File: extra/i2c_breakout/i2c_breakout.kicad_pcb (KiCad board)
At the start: 2 copper layers, 39.5 x 34.6 mm, 7 parts, among them J1 Conn_01x04_Socket, J2 Conn_01x04_Socket, J3 Conn_01x04_Socket, J4 Conn_01x04_Socket, U2 TLV1117-33

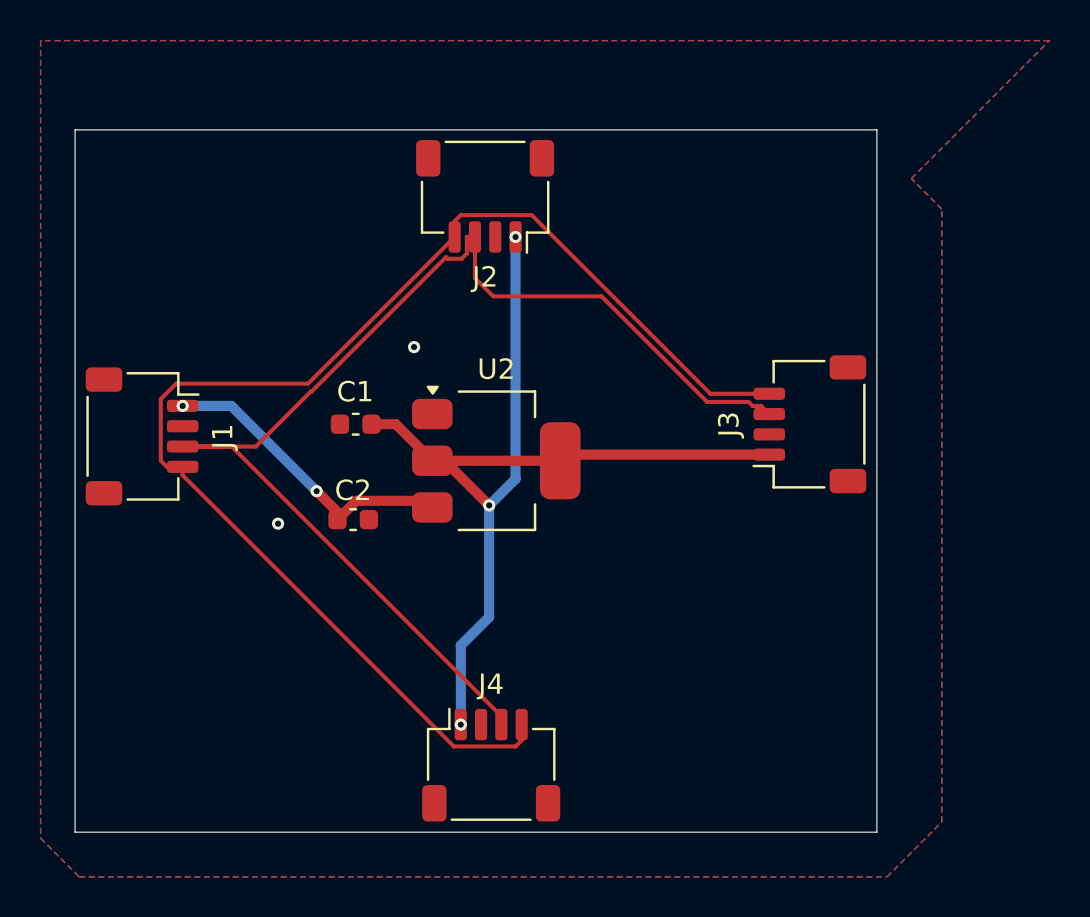
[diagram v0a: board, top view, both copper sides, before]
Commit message: Added jumper for power passthrough
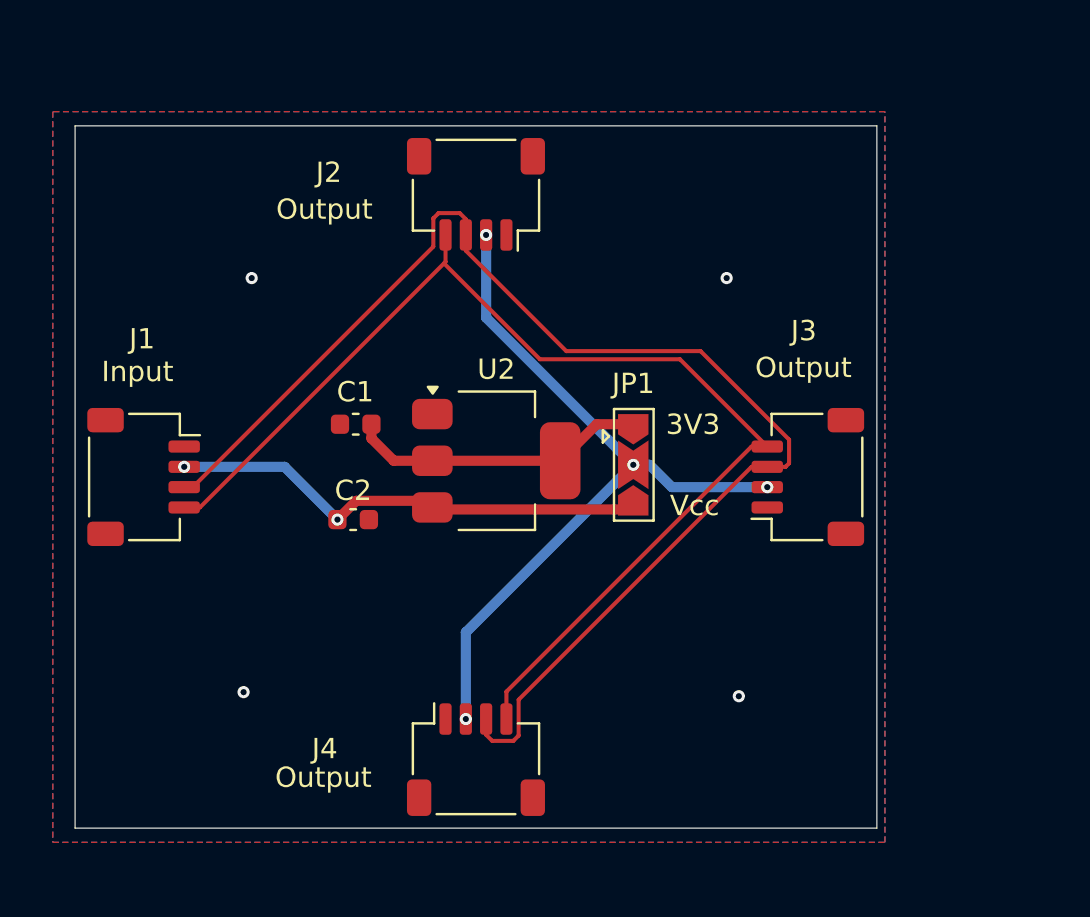
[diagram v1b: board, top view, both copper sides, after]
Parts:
- added JP1: SolderJumper_3_Open, Jumper:SolderJumper-3_P2.0mm_Open_TrianglePad1.0x1.5mm, F.Cu at (147.6, 66.4)
- moved J3 2.60 mm to (156.2, 67.0)
- moved J1 2.00 mm to (123.5, 67.0)
- moved J4 0.80 mm to (139.8, 80.9)
- moved J2 0.46 mm to (139.8, 53.1)
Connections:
- J1 pad 1: VCC -> GND
- J1 pad 2: GND -> VCC
- J2 pad 1: +3V3 -> GND
- J2 pad 2: GND -> VBUS
- J3 pad 1: +3V3 -> GND
- J3 pad 2: GND -> VBUS
- J4 pad 1: +3V3 -> GND
- J4 pad 2: GND -> VBUS
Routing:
- net VBUS: track 0.00 -> 37.3 mm, vias 0 -> 4
- net +3V3: track 49.3 -> 14.8 mm, vias 3 -> 0
- net VCC: track 15.4 -> 23.8 mm
- net /SCL: track 65.6 -> 58.1 mm
- net /SDA: track 60.1 -> 65.4 mm
- net GND: vias 2 -> 4
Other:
- board text added: "3V3"
- board text added: "Input"
- board text added: "Output"
- board text added: "Vcc"

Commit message: Updated silkscreen
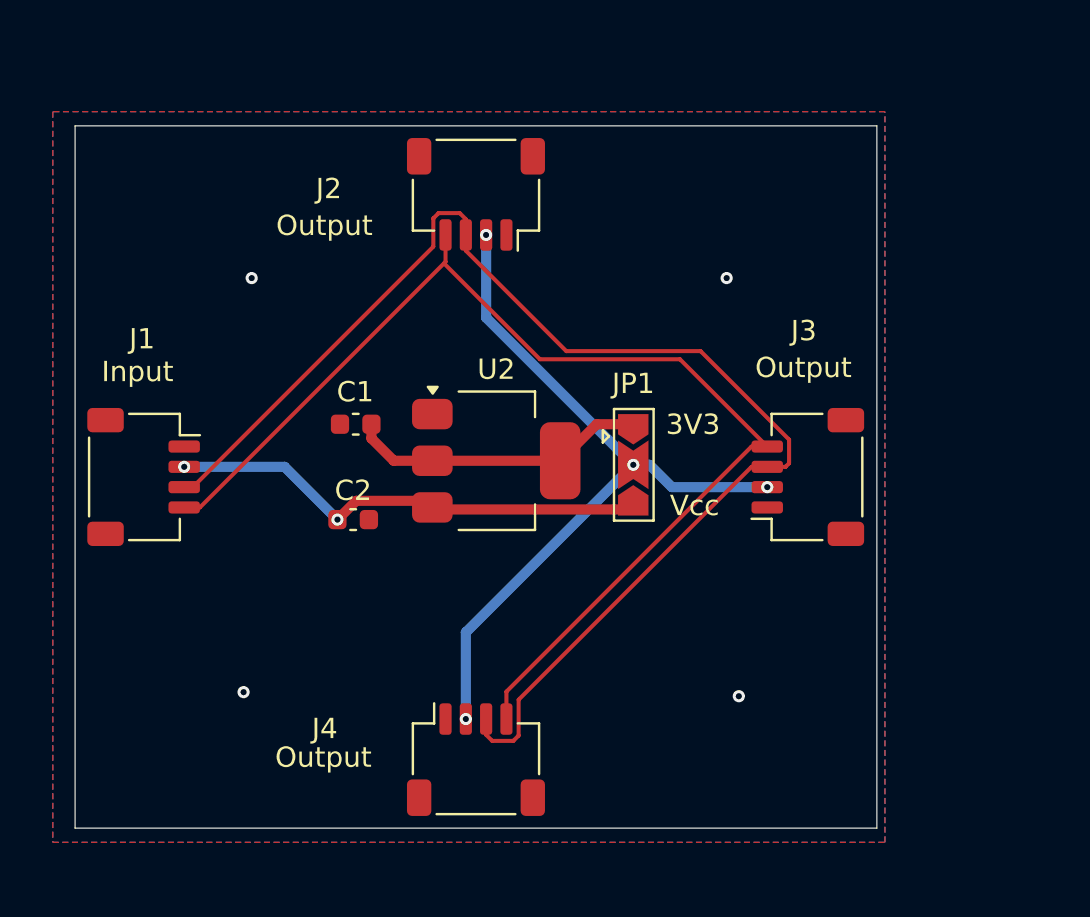
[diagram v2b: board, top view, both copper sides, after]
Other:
- board text added: "${ISSUE_DATE} ${TITLE} ${REVISION} ${COMPANY} ${COMMENT1}"
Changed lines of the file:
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@@
 	)
 	(paper "A4")
+	(title_block
+		(title "I2C Breakout Board")
+		(date "2025-08-26")
+		(rev "v1.0.0")
+		(company "jlab")
+		(comment 1 "John Madden")
+	)
 	(layers
 		(0 "F.Cu" signal)
@@
 		(tags "connector JST SH horizontal")
 		(property "Reference" "J2"
-			(at 7.25 1.075 0)
+			(at 7.25 0.275 0)
 			(layer "F.SilkS")
 			(effects
@@
 		(tags "connector JST SH horizontal")
 		(property "Reference" "J4"
-			(at -7.45 -0.535 0)
+			(at -7.45 -1.525 0)
 			(layer "F.SilkS")
 			(effects
@@
 	)
 	(gr_text "Output"
-		(at 129.95 82.39 0)
+		(at 129.95 81.4 0)
 		(layer "F.SilkS")
 		(effects
@@
 	)
 	(gr_text "Output"
-		(at 130 54.4 0)
+		(at 130 55.2 0)
 		(layer "F.SilkS")
 		(effects
@@
 		)
 	)
+	(gr_text "${ISSUE_DATE}\n${TITLE}\n${REVISION}\n${COMPANY}\n${COMMENT1}"
+		(at 155.6 61.4 0)
+		(layer "B.SilkS")
+		(effects
+			(font
+				(size 1 1)
+				(thickness 0.15)
+			)
+			(justify left bottom mirror)
+		)
+	)

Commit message: Added mounting holes
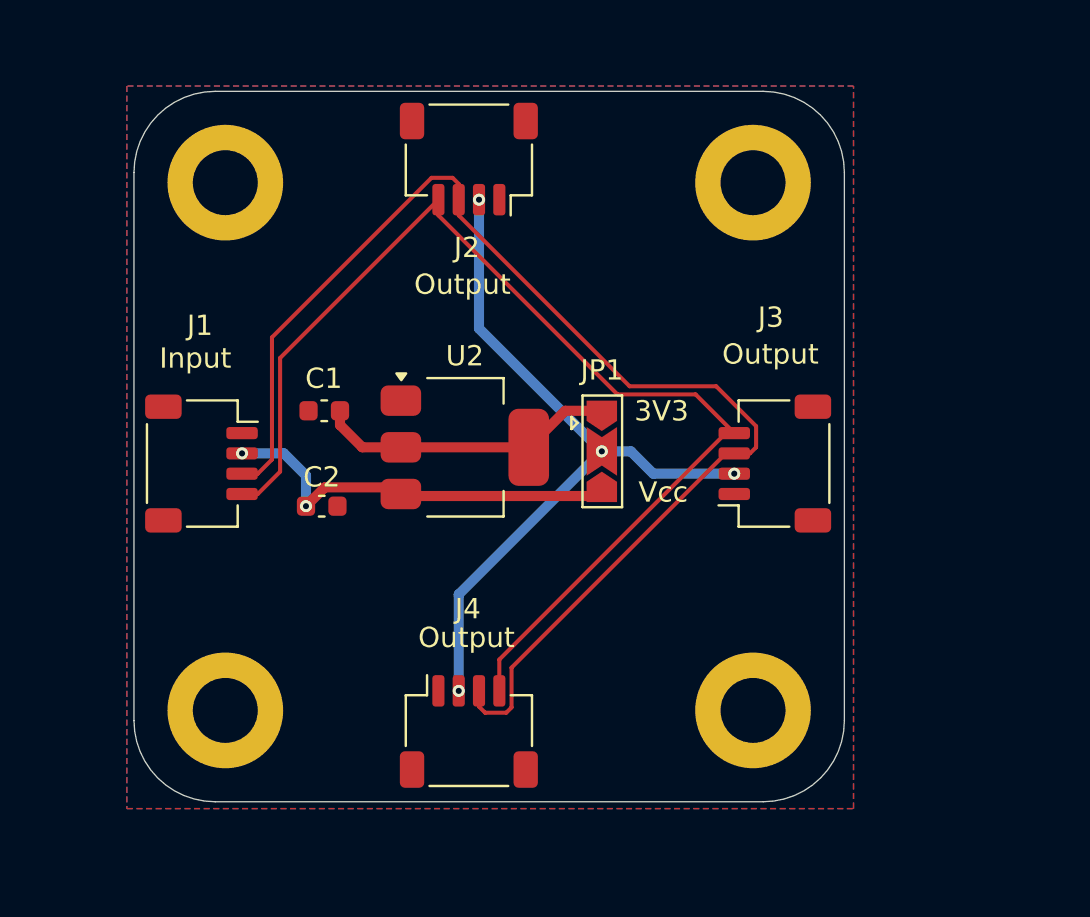
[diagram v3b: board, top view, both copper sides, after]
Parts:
- added H1: MountingHole_Pad, MountingHole:MountingHole_3.2mm_M3_ISO7380_Pad, F.Cu at (127.5, 52.5)
- added H2: MountingHole_Pad, MountingHole:MountingHole_3.2mm_M3_ISO7380_Pad, F.Cu at (153.5, 52.5)
- added H3: MountingHole_Pad, MountingHole:MountingHole_3.2mm_M3_ISO7380_Pad, F.Cu at (127.5, 78.5)
- added H4: MountingHole_Pad, MountingHole:MountingHole_3.2mm_M3_ISO7380_Pad, F.Cu at (153.5, 78.5)
- J1, J2, J3, J4: value Conn_01x04_Socket -> Conn_01x04_MountingPin
- moved J1 2.93 mm to (126.3, 66.3)
- moved J2 1.77 mm to (139.5, 51.3)
- moved J3 1.75 mm to (154.6, 66.3)
- moved C1 1.69 mm to (132.4, 63.7)
- moved C2 1.69 mm to (132.2, 68.4)
- moved JP1 1.69 mm to (146.1, 65.7)
- moved U2 1.69 mm to (139.3, 65.5)
- moved J4 1.43 mm to (139.5, 79.5)
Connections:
- J1 pad MP: (no net) -> GND
- J2 pad MP: (no net) -> GND
- J3 pad MP: (no net) -> GND
- J4 pad MP: (no net) -> GND
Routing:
- net VCC: track 23.8 -> 20.3 mm
- net /SDA: track 65.4 -> 63.0 mm
- net /SCL: track 58.1 -> 56.5 mm
- net VBUS: track 37.3 -> 36.6 mm
- net GND: vias 4 -> 0
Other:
- board size 39.5 x 34.6 mm -> 35 x 35 mm

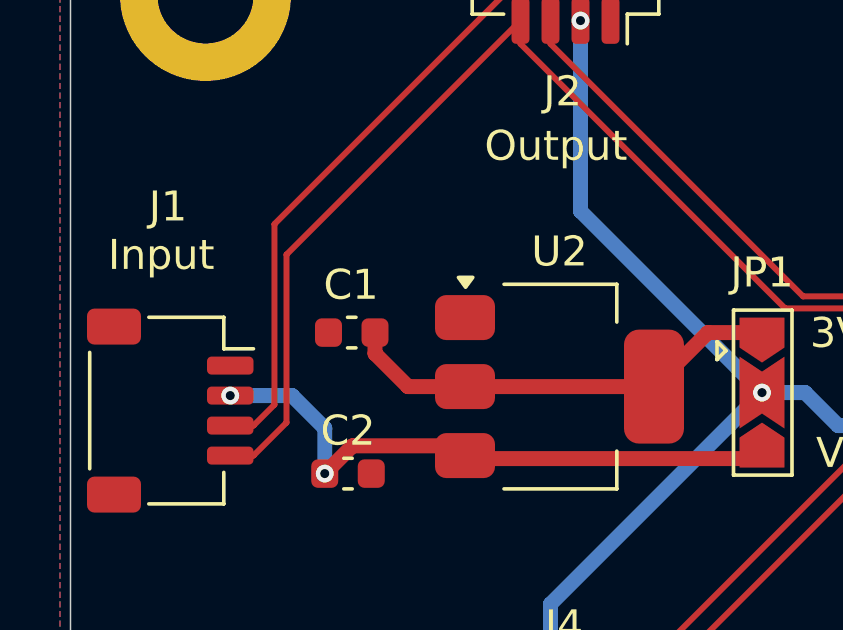
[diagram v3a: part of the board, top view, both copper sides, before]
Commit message: Updated 100uF cap to 0805
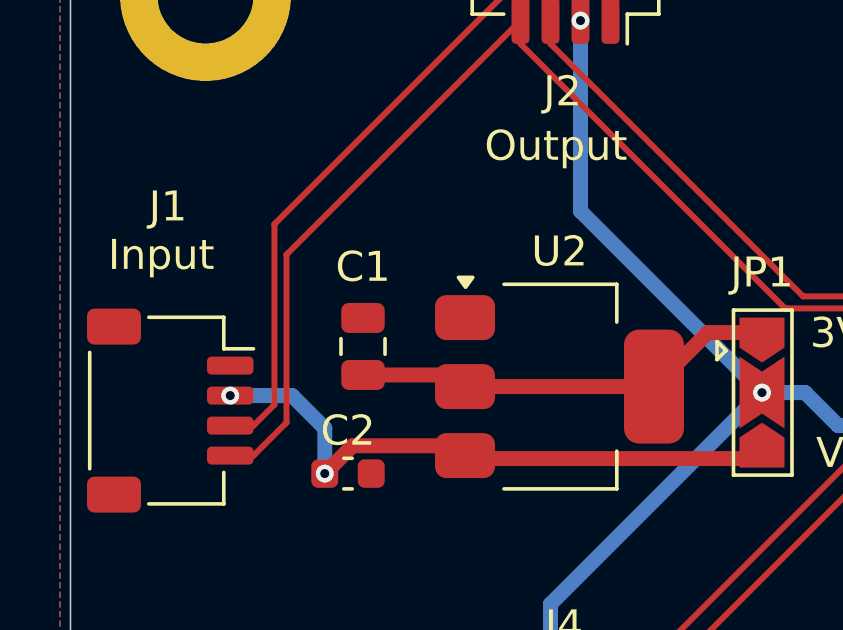
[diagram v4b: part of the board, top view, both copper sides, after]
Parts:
- C1: footprint Capacitor_SMD:C_0603_1608Metric -> Capacitor_SMD:C_0805_2012Metric
- moved C1 0.60 mm to (132.8, 64.2), turned to 90 degrees
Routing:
- net +3V3: track 14.8 -> 14.2 mm
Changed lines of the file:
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@@
+			)
+		)
+		(property "LCSC" ""
+			(at 0 0 0)
+			(unlocked yes)
+			(layer "F.Fab")
+			(hide yes)
+			(effects
+				(font
+					(size 1 1)
+					(thickness 0.15)
+				)
 			)
 		)
@@
 			)
 		)
+		(property "LCSC" "C160404"
+			(at 0 0 180)
+			(unlocked yes)
+			(layer "F.Fab")
+			(hide yes)
+			(effects
+				(font
+					(size 1 1)
+					(thickness 0.15)
+				)
+			)
+		)
 		(property ki_fp_filters "Connector*:*_1x??-1MP*")
 		(sheetname "/")
@@
 				(font
 					(size 1.27 1.27)
+					(thickness 0.15)
+				)
+			)
+		)
+		(property "LCSC" ""
+			(at 0 0 0)
+			(unlocked yes)
+			(layer "F.Fab")
+			(hide yes)
+			(effects
+				(font
+					(size 1 1)
 					(thickness 0.15)
 				)
@@
 			)
 		)
+		(property "LCSC" "C37359"
+			(at 0 0 0)
+			(unlocked yes)
+			(layer "F.Fab")
+			(hide yes)
+			(effects
+				(font
+					(size 1 1)
+					(thickness 0.15)
+				)
+			)
+		)
 		(property ki_fp_filters "SOT?223* TO?263* TO?252* TO?220*")
 		(sheetname "/")
@@
 			)
 		)
+		(property "LCSC" ""
+			(at 0 0 0)
+			(unlocked yes)
+			(layer "F.Fab")
+			(hide yes)
+			(effects
+				(font
+					(size 1 1)
+					(thickness 0.15)
+				)
+			)
+		)
 		(property ki_fp_filters "C_*")
 		(sheetname "/")
@@
 			)
 		)
+		(property "LCSC" "C160404"
+			(at 0 0 270)
+			(unlocked yes)
+			(layer "F.Fab")
+			(hide yes)
+			(effects
+				(font
+					(size 1 1)
+					(thickness 0.15)
+				)
+			)
+		)
 		(property ki_fp_filters "Connector*:*_1x??-1MP*")
 		(sheetname "/")
@@
 				(font
 					(size 1.27 1.27)
+					(thickness 0.15)
+				)
+			)
+		)
+		(property "LCSC" ""
+			(at 0 0 0)
+			(unlocked yes)
+			(layer "F.Fab")
+			(hide yes)
+			(effects
+				(font
+					(size 1 1)
 					(thickness 0.15)
 				)
@@
 			)
 		)
+		(property "LCSC" "C160404"
+			(at 0 0 90)
+			(unlocked yes)
+			(layer "F.Fab")
+			(hide yes)
+			(effects
+				(font
+					(size 1 1)
+					(thickness 0.15)
+				)
+			)
+		)
 		(property ki_fp_filters "Connector*:*_1x??-1MP*")
 		(sheetname "/")
@@
 			)
 		)
+		(property "LCSC" "C160404"
+			(at 0 0 0)
+			(unlocked yes)
+			(layer "F.Fab")
+			(hide yes)
+			(effects
+				(font
+					(size 1 1)
+					(thickness 0.15)
+				)
+			)
+		)
 		(property ki_fp_filters "Connector*:*_1x??-1MP*")
 		(sheetname "/")
@@
 		)
 	)
-	(footprint "Capacitor_SMD:C_0603_1608Metric"
+	(footprint "Capacitor_SMD:C_0805_2012Metric"
 		(layer "F.Cu")
-		(at 132.375 63.7375 180)
-		(descr "Capacitor SMD 0603 (1608 Metric), square (rectangular) end terminal, IPC-7351 nominal, (Body size source: IPC-SM-782 page 76, https://www.pcb-3d.com/wordpress/wp-content/uploads/ipc-sm-782a_amendment_1_and_2.pdf), generated with kicad-footprint-generator")
+		(at 132.75 64.2 90)
+		(descr "Capacitor SMD 0805 (2012 Metric), square (rectangular) end terminal, IPC-7351 nominal, (Body size source: IPC-SM-782 page 76, https://www.pcb-3d.com/wordpress/wp-content/uploads/ipc-sm-782a_amendment_1_and_2.pdf, https://docs.google.com/spreadsheets/d/1BsfQQcO9C6DZCsRaXUlFlo91Tg2WpOkGARC1WS5S8t0/edit?usp=sharing), generated with kicad-footprint-generator")
 		(tags "capacitor")
 		(property "Reference" "C1"
-			(at 0.025 1.59 0)
+			(at 2.65 0 180)
 			(layer "F.SilkS")
 			(effects
@@
 		)
 		(property "Value" "100uF"
-			(at 0 -1.51 0)
+			(at 0 1.68 90)
 			(layer "F.Fab")
 			(effects
@@
 		)
 		(property "Datasheet" "~"
-			(at 0 0 0)
+			(at 0 0 90)
 			(layer "F.Fab")
 			(hide yes)
@@
 		)
 		(property "Description" "Unpolarized capacitor"
-			(at 0 0 0)
+			(at 0 0 90)
 			(layer "F.Fab")
 			(hide yes)
@@
 				(font
 					(size 1.27 1.27)
+					(thickness 0.15)
+				)
+			)
+		)
+		(property "LCSC" ""
+			(at 0 0 90)
+			(unlocked yes)
+			(layer "F.Fab")
+			(hide yes)
+			(effects
+				(font
+					(size 1 1)
 					(thickness 0.15)
 				)
@@
 		(attr smd)
 		(fp_line
-			(start -0.14058 0.51)
-			(end 0.14058 0.51)
-			(stroke
-				(width 0.12)
-				(type solid)
-			)
-			(layer "F.SilkS")
-		)
-		(fp_line
-			(start -0.14058 -0.51)
-			(end 0.14058 -0.51)
-			(stroke
-				(width 0.12)
-				(type solid)
-			)
-			(layer "F.SilkS")
-		)
-		(fp_line
-			(start 1.48 0.73)
-			(end -1.48 0.73)
-			(stroke
-				(width 0.05)
-				(type solid)
-			)
-			(layer "F.CrtYd")
-		)
-		(fp_line
-			(start 1.48 -0.73)
-			(end 1.48 0.73)
-			(stroke
-				(width 0.05)
-				(type solid)
-			)
-			(layer "F.CrtYd")
-		)
-		(fp_line
-			(start -1.48 0.73)
-			(end -1.48 -0.73)
-			(stroke
-				(width 0.05)
-				(type solid)
-			)
-			(layer "F.CrtYd")
-		)
-		(fp_line
-			(start -1.48 -0.73)
-			(end 1.48 -0.73)
-			(stroke
-				(width 0.05)
-				(type solid)
-			)
-			(layer "F.CrtYd")
-		)
-		(fp_line
-			(start 0.8 0.4)
-			(end -0.8 0.4)
-			(stroke
-				(width 0.1)
-				(type solid)
-			)
-			(layer "F.Fab")
-		)
-		(fp_line
-			(start 0.8 -0.4)
-			(end 0.8 0.4)
-			(stroke
-				(width 0.1)
-				(type solid)
-			)
-			(layer "F.Fab")
-		)
-		(fp_line
-			(start -0.8 0.4)
-			(end -0.8 -0.4)
-			(stroke
-				(width 0.1)
-				(type solid)
-			)
-			(layer "F.Fab")
-		)
-		(fp_line
-			(start -0.8 -0.4)
-			(end 0.8 -0.4)
+			(start -0.261252 -0.735)
+			(end 0.261252 -0.735)
+			(stroke
+				(width 0.12)
+				(type solid)
+			)
+			(layer "F.SilkS")
+		)
+		(fp_line
+			(start -0.261252 0.735)
+			(end 0.261252 0.735)
+			(stroke
+				(width 0.12)
+				(type solid)
+			)
+			(layer "F.SilkS")
+		)
+		(fp_line
+			(start 1.7 -0.98)
+			(end 1.7 0.98)
+			(stroke
+				(width 0.05)
+				(type solid)
+			)
+			(layer "F.CrtYd")
+		)
+		(fp_line
+			(start -1.7 -0.98)
+			(end 1.7 -0.98)
+			(stroke
+				(width 0.05)
+				(type solid)
+			)
+			(layer "F.CrtYd")
+		)
+		(fp_line
+			(start 1.7 0.98)
+			(end -1.7 0.98)
+			(stroke
+				(width 0.05)
+				(type solid)
+			)
+			(layer "F.CrtYd")
+		)
+		(fp_line
+			(start -1.7 0.98)
+			(end -1.7 -0.98)
+			(stroke
+				(width 0.05)
+				(type solid)
+			)
+			(layer "F.CrtYd")
+		)
+		(fp_line
+			(start 1 -0.625)
+			(end 1 0.625)
+			(stroke
+				(width 0.1)
+				(type solid)
+			)
+			(layer "F.Fab")
+		)
+		(fp_line
+			(start -1 -0.625)
+			(end 1 -0.625)
+			(stroke
+				(width 0.1)
+				(type solid)
+			)
+			(layer "F.Fab")
+		)
+		(fp_line
+			(start 1 0.625)
+			(end -1 0.625)
+			(stroke
+				(width 0.1)
+				(type solid)
+			)
+			(layer "F.Fab")
+		)
+		(fp_line
+			(start -1 0.625)
+			(end -1 -0.625)
 			(stroke
 				(width 0.1)
@@
 		)
 		(fp_text user "${REFERENCE}"
-			(at 0 0 0)
-			(layer "F.Fab")
-			(effects
-				(font
-					(size 0.4 0.4)
-					(thickness 0.06)
+			(at 0 0 90)
+			(layer "F.Fab")
+			(effects
+				(font
+					(size 0.5 0.5)
+					(thickness 0.08)
 				)
 			)
 		)
 		(pad "1" smd roundrect
-			(at -0.775 0 180)
-			(size 0.9 0.95)
+			(at -0.95 0 90)
+			(size 1 1.45)
 			(layers "F.Cu" "F.Mask" "F.Paste")
 			(roundrect_rratio 0.25)
@@
 		)
 		(pad "2" smd roundrect
-			(at 0.775 0 180)
-			(size 0.9 0.95)
+			(at 0.95 0 90)
+			(size 1 1.45)
 			(layers "F.Cu" "F.Mask" "F.Paste")
 			(roundrect_rratio 0.25)
@@
 		)
 		(embedded_fonts no)
-		(model "${KICAD9_3DMODEL_DIR}/Capacitor_SMD.3dshapes/C_0603_1608Metric.step"
+		(model "${KICAD9_3DMODEL_DIR}/Capacitor_SMD.3dshapes/C_0805_2012Metric.step"
 			(offset
 				(xyz 0 0 0)
@@
 				(font
 					(size 1.27 1.27)
+					(thickness 0.15)
+				)
+			)
+		)
+		(property "LCSC" ""
+			(at 0 0 270)
+			(unlocked yes)
+			(layer "F.Fab")
+			(hide yes)
+			(effects
+				(font
+					(size 1 1)
 					(thickness 0.15)
 				)
@@
 			)
 		)
+		(property "LCSC" ""
+			(at 0 0 0)
+			(unlocked yes)
+			(layer "F.Fab")
+			(hide yes)
+			(effects
+				(font
+					(size 1 1)
+					(thickness 0.15)
+				)
+			)
+		)
 		(property ki_fp_filters "MountingHole*Pad*")
 		(sheetname "/")
@@
 	)
 	(segment
-		(start 133.15 64.4375)
-		(end 134.25 65.5375)
+		(start 135.7625 65.15)
+		(end 136.15 65.5375)
 		(width 0.5)
 		(layer "F.Cu")
@@
 	)
 	(segment
-		(start 133.15 63.7375)
-		(end 133.15 64.4375)
+		(start 132.75 65.15)
+		(end 135.7625 65.15)
 		(width 0.5)
 		(layer "F.Cu")
-		(net 1)
-	)
-	(segment
-		(start 134.25 65.5375)
-		(end 136.15 65.5375)
-		(width 0.5)
-		(layer "F.Cu")
